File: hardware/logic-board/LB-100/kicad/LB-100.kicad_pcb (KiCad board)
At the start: 4 copper layers, 100 x 70 mm, 112 parts, among them Q18 BC847BQ-7-F 12V OPTION, Q19 BC847BQ-7-F 12V OPTION, U1 STM32H563VIT6, U10 BMI270, U11 VEML7700-TT, U12 TPS22918TDBVRQ1, U13 TPS22918TDBVRQ1, U14 SN74LVC1G17QDBVRQ1, U15 SN74LVC1G125QDBVRQ1, U16 SN74LVC1G125QDBVRQ1, U17 SN74LVC1G125QDBVRQ1, U18 SN74LVC1G17QDBVRQ1, U19 SN74LVC1G17QDBVRQ1, U2 XC6220B331MR-G, U3 TCA9539QPWRQ1, U4 TJA1051TK/3,118, U5 TJA1021T/20/CM,118, U6 SP3485EN-L/TR, U7 E73-2G4M08S1C, U8 FM24CL64B-GTR, U9 DS3231MZ+TRL, Y1 ABM8AIG-25.000MHZ-12-2Z-T3, Y2 ABS07AIG-32.768kHz-7-T

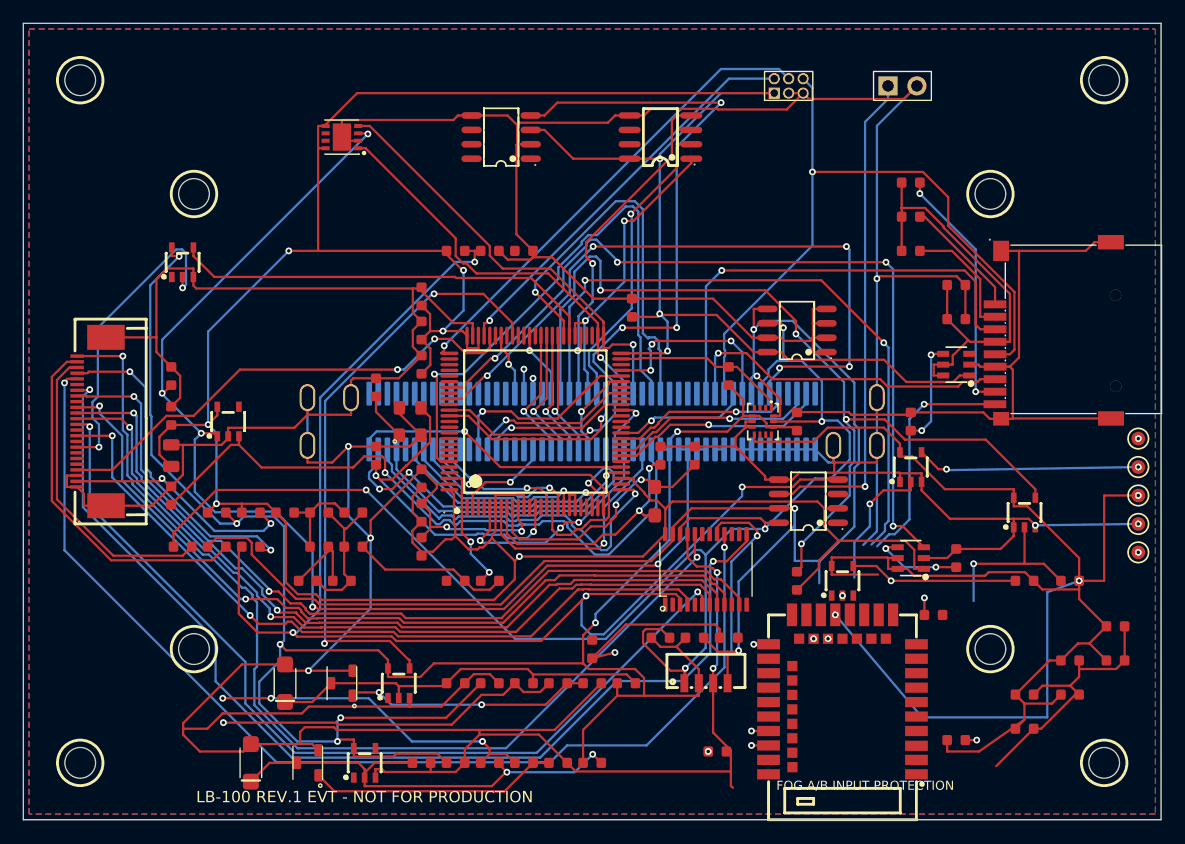
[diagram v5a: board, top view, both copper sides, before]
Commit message: finish LB-100 EVT routing and fab package
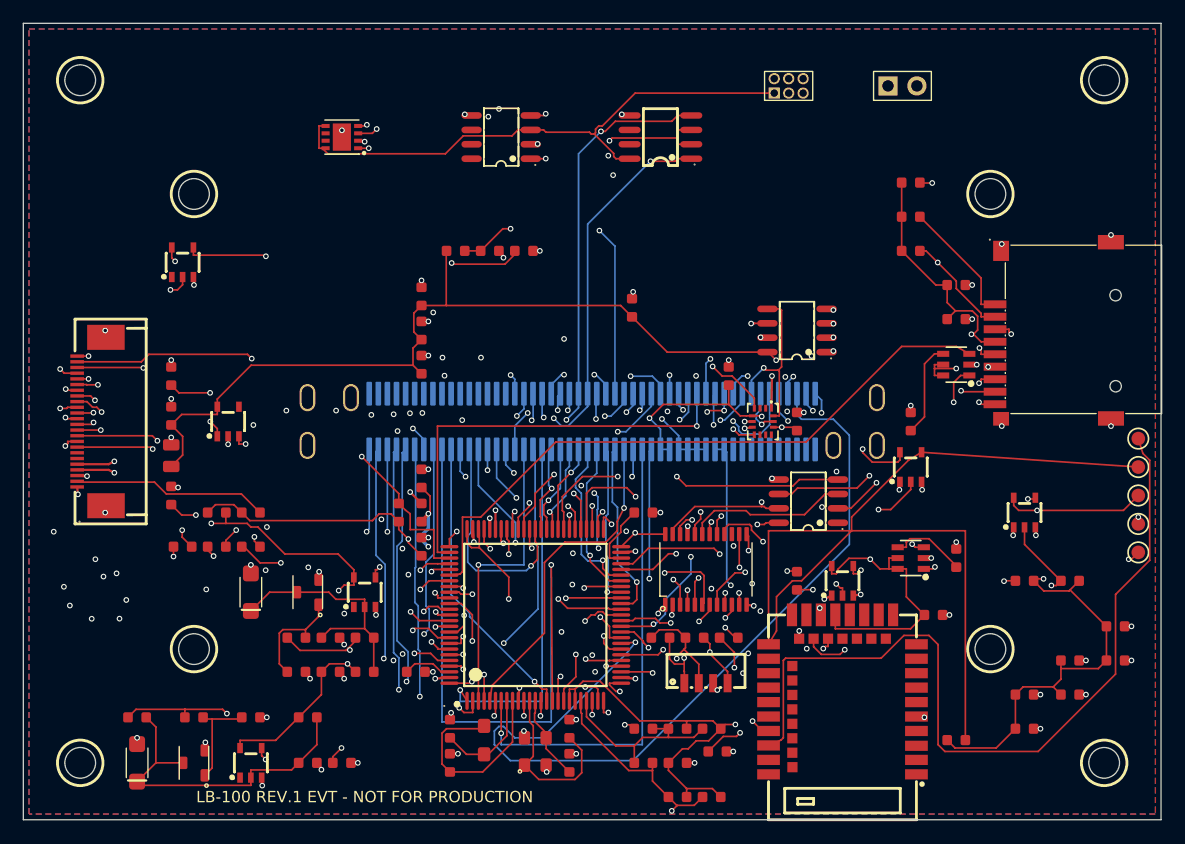
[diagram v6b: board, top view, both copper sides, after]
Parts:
- moved C28 37.6 mm to (57.5, 68.0)
- moved C29 37.6 mm to (60.5, 68.0)
- moved C4 36.8 mm to (57.5, 62.0)
- moved C5 36.8 mm to (60.5, 62.0)
- moved FB1 36.8 mm to (54.5, 62.0)
- moved C12 34.5 mm to (37.5, 65.0)
- moved C9 34.5 mm to (48.0, 62.0)
- moved R16 34.3 mm to (54.5, 65.0)
- moved R17 34.3 mm to (57.5, 65.0)
- moved C10 31.9 mm to (48.0, 65.0)
- moved R27 31.3 mm to (10.0, 61.0)
- moved Y1 31.0 mm to (45.0, 64.0)
- moved C11 30.3 mm to (37.5, 62.0)
- moved R28 29.3 mm to (15.0, 61.0)
- moved R29 27.3 mm to (20.0, 61.0)
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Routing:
- net GND: track 682.7 -> 66.6 mm, vias 10 -> 94
- net CH_LED_10: track 0.00 -> 79.5 mm, vias 0 -> 3
- net CH_LED_7: track 0.00 -> 78.1 mm, vias 0 -> 3
- net CH_LED_2: track 0.00 -> 71.6 mm, vias 0 -> 3
- net MICROSD_CS_N: track 10.9 -> 80.3 mm, vias 0 -> 3
- net RADIO_SENSOR_3V3: track 181.2 -> 122.7 mm, vias 4 -> 5
- net TEMP_PCB: track 18.2 -> 75.4 mm
- net MICROSD_PWR_EN: track 0.00 -> 57.0 mm
- net PB_SPI_SCK: track 61.9 -> 118.4 mm, vias 1 -> 8
- net CAN1_TX_ROUTE: track 0.00 -> 51.4 mm, vias 0 -> 3
- net PB_SPI_MISO: track 29.5 -> 80.1 mm, vias 1 -> 4
- net ADC_REF: track 7.24 -> 56.6 mm, vias 0 -> 2
- net STATUS_RGB_DATA: track 0.00 -> 49.4 mm, vias 0 -> 3
- net VBAT_SENSE: track 0.00 -> 44.9 mm, vias 0 -> 3
- net LIN_RX: track 17.8 -> 61.2 mm, vias 1 -> 5
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- added copper zone on In4.Cu, net GND
- removed copper zone on In1.Cu, net GND
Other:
- copper layers 4 -> 6
- board text added: "STACKUP JLC06161H-3313 / 6L / 1.6 mm"
